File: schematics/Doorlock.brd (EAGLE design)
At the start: 79.7 x 80 mm, 33 parts, among them IC1 AT90S2313P, IC2 MAX232, K1 FRS1B, K2 FRS1B

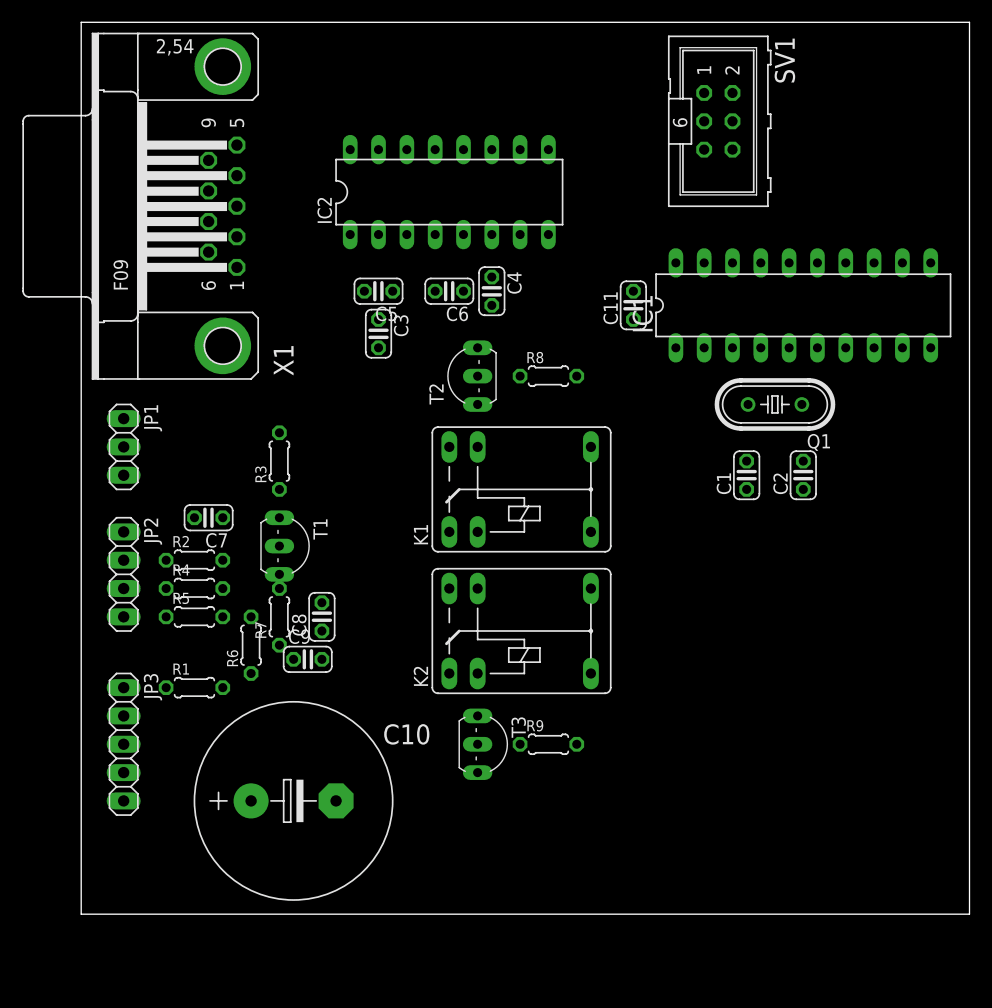
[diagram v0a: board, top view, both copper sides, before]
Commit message: First steps towards Raspberry Pi doorlock hat
Signed-off-by: Ralf Ramsauer <ralf@binary-kitchen.de>
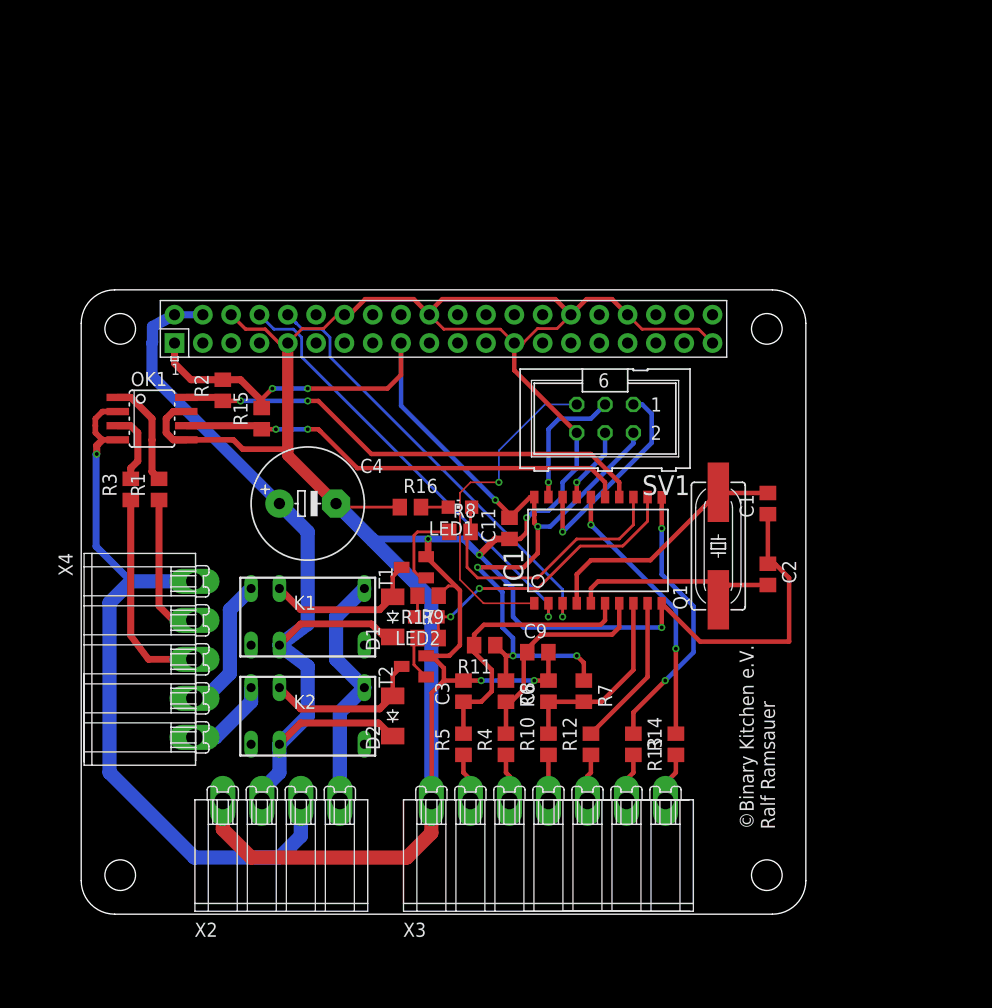
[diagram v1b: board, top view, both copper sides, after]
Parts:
- removed C10: (no value), rcl:E7,5-18
- removed C5, C6: 1u, rcl:C025-024X044
- removed C7: 100n, rcl:C025-024X044
- removed IC2: MAX232, maxim:DIL16
- removed JP1: (no value), pinhead:1X03
- removed JP2: (no value), pinhead:1X04
- removed JP3: (no value), pinhead:1X05
- removed T3: (no value), transistor:TO92-CBE
- added D1, D2: CGRM4002-G, diode:SOD-123_MINI-SMA
- added LED1, LED2: (no value), led:CHIP-LED0805
- added OK1: ILD205, optocoupler:SOIC08
- added R10, R15: 1k, rcl:R0805
- added R11: 10k, rcl:R0805
- added R12, R13, R14, R16, R17: 100, rcl:R0805
- added X2: RIA182-04, con-ria182:RIA182-04
- added X3: RIA182-07, con-ria182:RIA182-07
- added X4: RIA182-05, con-ria182:RIA182-05
- C1, C11, C2, C8, C9: device rcl:C025-024X044 -> rcl:C0805
- C3: value 1u -> 100n; device rcl:C025-024X044 -> rcl:C0805
- C4: value 1u -> RAD FC 1.200/16; device rcl:C025-024X044 -> rcl:E5-10,5
- IC1: value AT90S2313P -> AT90S2313S; device atmel:DIL20 -> atmel:SO20L
- K1, K2: value FRS1B -> G5V1; device relay:FRS1B -> relay:G5V1
- Q1: device crystal:HC49/S -> crystal:HC49UP
- R1, R4, R5, R6, R7, R8, R9: device rcl:0204/5 -> rcl:R0805
- R2, R3: value 10k -> 1k; device rcl:0204/5 -> rcl:R0805
- T1, T2: device transistor:TO92-CBE -> transistor:SOT23-BEC
- X1: value (none) -> RASPI_BOARD_B+#_H; device con-subd:F09HP -> raspberrypi_bastelstube_v13:RASPI_BOARD_B+HAT
- moved X1 64.8 mm to (0.00, 0.00), turned to 0 degrees
- moved C3 33.0 mm to (34.3, 20.0), turned to 90 degrees
- moved R4 31.2 mm to (38.1, 15.2), turned to 90 degrees
- moved IC1 28.8 mm to (45.7, 33.0)
- moved SV1 28.5 mm to (47.0, 44.5), turned to 180 degrees
- moved R7 28.1 mm to (45.1, 20.0), turned to 270 degrees
- moved R5 26.7 mm to (34.3, 15.2), turned to 90 degrees
- moved T2 26.7 mm to (29.8, 22.2)
- moved C4 25.2 mm to (20.3, 36.8), turned to 0 degrees
- moved R6 23.2 mm to (38.1, 20.0), turned to 270 degrees
- moved C11 22.9 mm to (38.4, 34.6)
- moved C8 21.4 mm to (41.9, 20.0)
- moved C9 20.6 mm to (41.0, 23.5)
- moved K1 19.1 mm to (20.3, 26.7)
- moved R1 18.1 mm to (6.99, 38.1), turned to 90 degrees
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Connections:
- removed net 12VAC: JP3.3
- removed net BUTTON_LOCK: C9.1, IC1.6, R5.2, R6.2
- removed net BUTTON_UNLOCK: C8.1, IC1.7, R4.2, R7.2
- removed net N$15: C6.1, IC2.5
- removed net N$18: C5.2, IC2.1
- removed net N$19: JP3.1, R1.1
- removed net N$23: K2.S
- removed net STATUS: IC1.14, R1.2
- new net +5V: C4.+, D1.C, D2.C, K1.2, K2.2, X1.2, X1.4, X2.2
- new net BUTTON_GREEN: C8.1, IC1.8, R10.2, R7.2
- new net BUTTON_RED: C3.1, IC1.6, R11.2, R5.2
- new net BUTTON_YELLOW: C9.1, IC1.7, R4.2, R6.2
- new net GND2: OK1.2, OK1.4, X2.3, X4.1
- new net LED_GREEN: IC1.16, R14.2
- new net LED_RED: IC1.9, R12.2
- new net LED_YELLOW: IC1.11, R13.1
- new net RXD: IC1.2, X1.8
- new net TUERSTATUS: IC1.14, OK1.8, R2.1
- new net TXD: IC1.3, X1.10
- net +12V: now also K1.6, K2.6, X2.4; no longer JP3.2
- net BOLZEN: now also IC1.13, LED1.A; no longer IC1.12
- net BOLZEN_OUT: now also K1.10, X4.4; no longer JP2.3, K1.S
- net EMERGENCY_UNLOCK: now also IC1.15, OK1.6, R15.1; no longer IC1.8, R3.1, T1.C
- net GND: now also C3.2, C4.-, OK1.5, OK1.7, R16.1, R17.1, X1.14, X1.20, X1.25, X1.30, X1.34, X1.39, X1.6, X1.9, X2.1, X3.1; no longer C10.-, C4.2, C7.1, IC2.15, JP1.1, JP2.1, JP3.5, T3.E, X1.5
- net N$10: now also R1.1, X4.2; no longer JP2.2, R2.1
- net N$11: now also R13.2, X3.6; no longer C3.1, IC2.2
- net N$12: now also R14.1, X3.7; no longer C4.1, IC2.6
- net N$13: now also R3.1, X4.3; no longer IC1.2, IC2.11
- net N$14: now also OK1.1, R1.2; no longer IC1.3, IC2.12
- net N$16: now also LED1.C, R16.2; no longer C6.2, IC2.4
- net N$17: now also LED2.C, R17.2; no longer C5.1, IC2.3
- net N$20: now also X3.3; no longer JP1.2
- net N$21: now also X3.2; no longer JP1.3
- net N$24: now also D2.A, K2.9, T2.C; no longer K2.2, T3.C
- net N$25: now also D1.A, K1.9, T1.C; no longer K1.1, T2.C
- net N$27: now also T1.B; no longer T2.B
- net N$28: now also T2.B; no longer T3.B
- net N$4: now also OK1.3, R3.2; no longer C7.2, R2.2, T1.B
- net N$8: now also R10.1, X3.4; no longer IC2.14, X1.2
- net N$9: now also R12.1, X3.5; no longer IC2.13, X1.3
- net SCHNAPPER: now also IC1.12, LED2.A; no longer IC1.13
- net SCHNAPPER_OUT: now also K2.10, X4.5; no longer JP2.4
- net VCC: now also R11.1, R15.2, R2.2, X1.1, X1.17; no longer C10.+, C3.2, IC2.16, JP3.4, K1.2, K2.1, R3.2
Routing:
- net GND: track 0.00 -> 285.9 mm, vias 0 -> 6
- net VCC: track 0.00 -> 96.1 mm, vias 0 -> 7
- net +5V: track 0.00 -> 80.2 mm
- net GND2: track 0.00 -> 68.0 mm, vias 0 -> 1
- net TUERSTATUS: track 0.00 -> 43.3 mm, vias 0 -> 2
- net EMERGENCY_UNLOCK: track 0.00 -> 41.0 mm, vias 0 -> 2
- net RXD: track 0.00 -> 40.1 mm, vias 0 -> 1
- net TXD: track 0.00 -> 39.6 mm, vias 0 -> 1
- net N$3: track 0.00 -> 30.8 mm, vias 0 -> 1
- net SCHNAPPER: track 0.00 -> 26.4 mm, vias 0 -> 2
- net BOLZEN: track 0.00 -> 25.3 mm
- net BUTTON_RED: track 0.00 -> 25.3 mm
- net LED_YELLOW: track 0.00 -> 24.6 mm, vias 0 -> 2
- net LED_GREEN: track 0.00 -> 24.4 mm, vias 0 -> 2
- net N$6: track 0.00 -> 22.9 mm
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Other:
- board size 79.7 x 80 mm -> 65 x 56 mm
- board text added: "©Binary Kitchen e.V. Ralf Ramsauer"

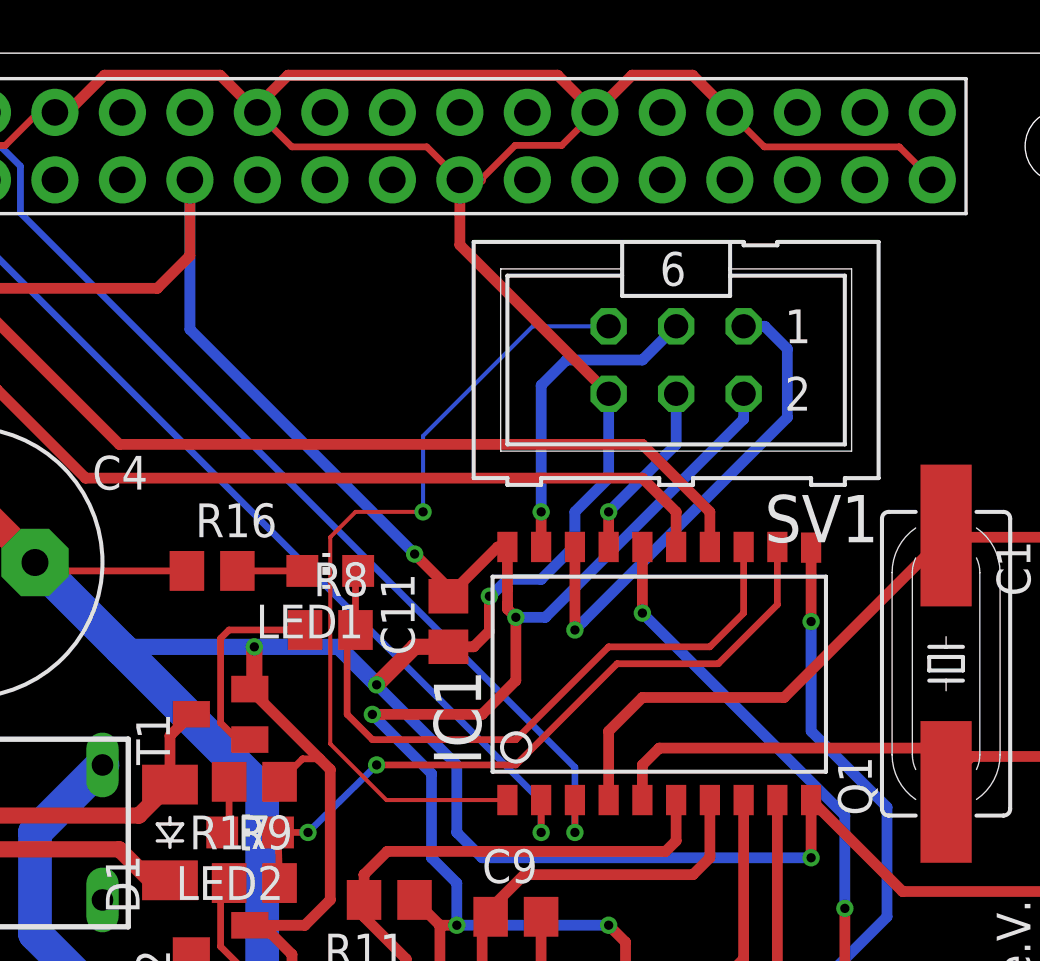
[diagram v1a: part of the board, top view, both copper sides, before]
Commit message: Remove ISP adapter
Let's flash the device with the Raspberry Pi :-)
... But add an Jumper for the reset line.

Signed-off-by: Ralf Ramsauer <ralf@binary-kitchen.de>
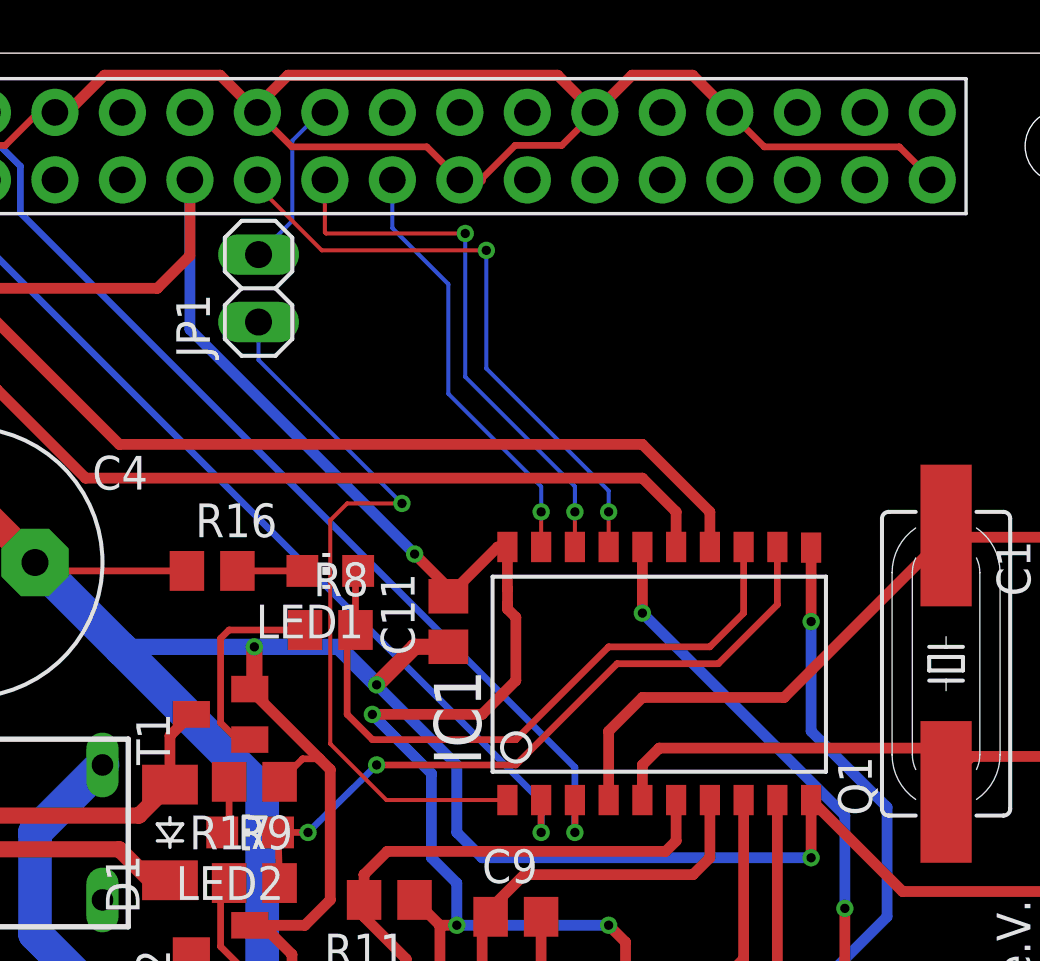
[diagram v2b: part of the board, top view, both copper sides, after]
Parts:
- removed SV1: (no value), con-harting-ml:ML6
- added JP1: (no value), pinhead:1X02
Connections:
- removed net N$2: IC1.19, SV1.3
- removed net N$3: IC1.1, SV1.5
- removed net N$5: IC1.17, SV1.4
- new net MISO: IC1.18, X1.21
- new net MOSI: IC1.17, X1.19
- new net RESET: JP1.2, X1.22
- new net SCK: IC1.19, X1.23
- net GND: no longer SV1.6
- net N$1: now also IC1.1, JP1.1; no longer IC1.18, SV1.1
- net VCC: no longer SV1.2
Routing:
- net N$3: track 30.8 -> 0.00 mm, vias 1 -> 0
- net GND: track 285.9 -> 262.2 mm, vias 6 -> 5
- net MOSI: track 0.00 -> 22.9 mm, vias 0 -> 2
- net MISO: track 0.00 -> 20.8 mm, vias 0 -> 2
- net SCK: track 0.00 -> 16.1 mm, vias 0 -> 1
- net VCC: track 96.1 -> 83.5 mm, vias 7 -> 6
- net N$2: track 12.1 -> 0.00 mm, vias 1 -> 0
- net N$1: track 19.0 -> 28.0 mm
- net N$5: track 6.82 -> 0.00 mm, vias 1 -> 0
- net RESET: track 0.00 -> 6.48 mm

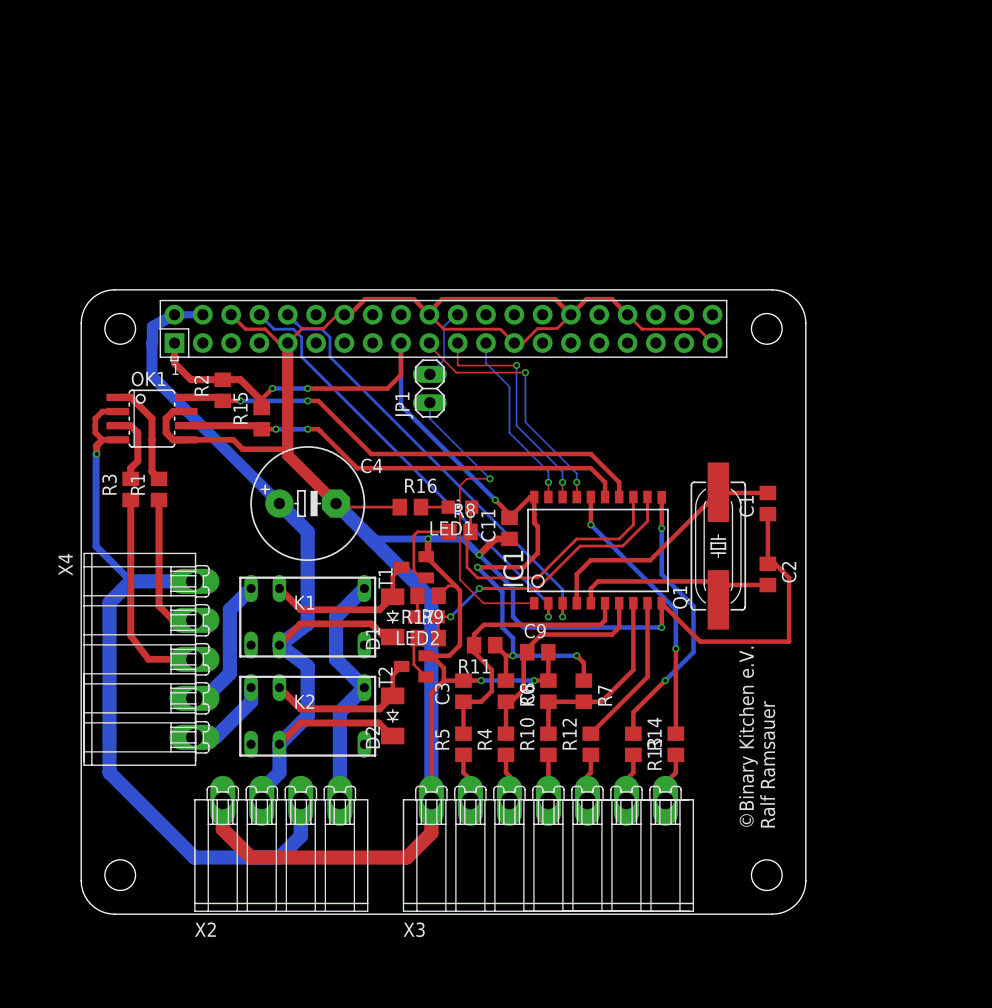
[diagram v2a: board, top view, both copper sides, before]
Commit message: schematics: improve schematics
  - Use RJ45 instead for buttons/LEDs
  - Use SMD capacitor

Signed-off-by: Ralf Ramsauer <ralf@binary-kitchen.de>
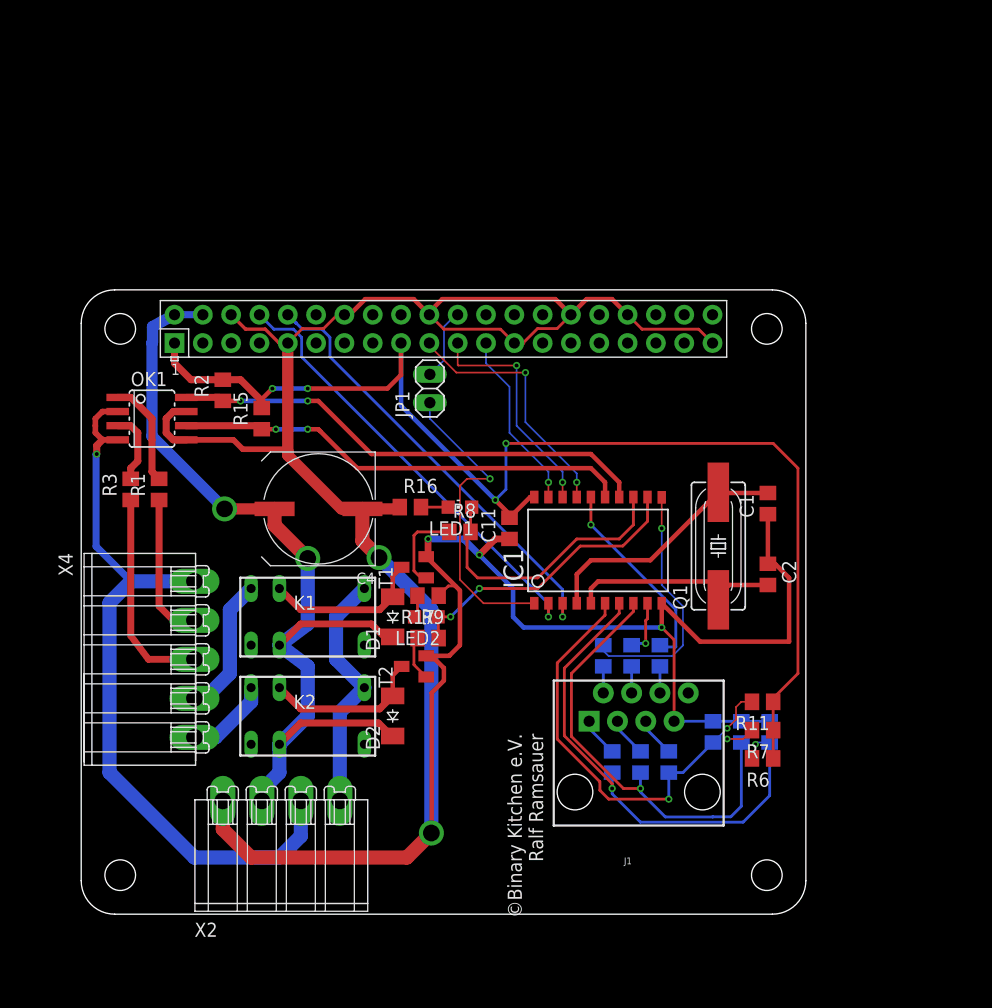
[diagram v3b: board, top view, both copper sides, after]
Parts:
- removed X3: RIA182-07, con-ria182:RIA182-07
- added J1: RJ45, SparkFun-Connectors:RJ45-8
- C4: value RAD FC 1.200/16 -> VF1000/10K-G; device rcl:E5-10,5 -> rcl:UD-10X10_NICHICON
- moved R11 25.4 mm to (61.1, 19.1)
- moved R6 23.8 mm to (61.1, 14.0), turned to 180 degrees
- moved C3 22.7 mm to (56.7, 16.4), flipped to the bottom
- moved C9 22.0 mm to (61.8, 16.4), flipped to the bottom, turned to 90 degrees
- moved R5 18.5 mm to (52.7, 13.7), flipped to the bottom, turned to 270 degrees
- moved C8 17.7 mm to (59.2, 16.4), flipped to the bottom
- moved R7 16.4 mm to (61.1, 16.5), turned to 180 degrees
- moved R4 9.66 mm to (47.6, 13.7), flipped to the bottom, turned to 270 degrees
- moved R12 8.74 mm to (49.4, 23.2), flipped to the bottom
- moved R10 8.41 mm to (50.2, 13.7), flipped to the bottom, turned to 270 degrees
- moved R13 8.38 mm to (46.8, 23.2), flipped to the bottom
- moved R14 8.07 mm to (51.9, 23.2), flipped to the bottom
- moved C4 1.06 mm to (21.3, 36.4), turned to 180 degrees
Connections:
- removed net N$12: R14.1, X3.7
- new net N$2: J1.6, R14.1
- net GND: now also J1.7; no longer X3.1
- net N$11: now also J1.2; no longer X3.6
- net N$20: now also J1.1; no longer X3.3
- net N$21: now also J1.5; no longer X3.2
- net N$8: now also J1.3; no longer X3.4
- net N$9: now also J1.4; no longer X3.5
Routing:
- net VCC: track 83.5 -> 110.3 mm, vias 6 -> 4
- net BUTTON_GREEN: track 17.6 -> 44.2 mm, vias 0 -> 2
- net BUTTON_YELLOW: track 19.9 -> 46.0 mm, vias 0 -> 2
- net BUTTON_RED: track 25.3 -> 39.8 mm, vias 0 -> 2
- net LED_RED: track 13.8 -> 5.00 mm, vias 0 -> 1
- net LED_GREEN: track 24.4 -> 18.1 mm, vias 2 -> 1
- net N$12: track 4.52 -> 0.00 mm
- net +5V: track 80.2 -> 82.9 mm, vias 0 -> 2
- net N$2: track 0.00 -> 2.38 mm
- net LED_YELLOW: track 24.6 -> 22.3 mm, vias 2 -> 1
- net GND: track 262.2 -> 264.3 mm
- net N$11: track 4.39 -> 2.38 mm
- net N$9: track 4.26 -> 2.38 mm
- net N$21: track 4.39 -> 3.56 mm
- net N$20: track 4.26 -> 3.56 mm
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
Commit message: schematics: Update Resistor values
Signed-off-by: Ralf Ramsauer <ralf@binary-kitchen.de>
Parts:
- R12, R13: value 100 -> 220
- R14: value 100 -> 0
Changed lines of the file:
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@@
 <element name="R10" library="rcl" package="R0805" value="1k" x="50.165" y="13.6525" rot="MR270"/>
 <element name="R11" library="rcl" package="R0805" value="10k" x="61.11875" y="19.05" rot="R180"/>
-<element name="R12" library="rcl" package="R0805" value="100" x="49.37125" y="23.1775" rot="MR90"/>
-<element name="R13" library="rcl" package="R0805" value="100" x="46.83125" y="23.1775" rot="MR270"/>
-<element name="R14" library="rcl" package="R0805" value="100" x="51.91125" y="23.1775" rot="MR90"/>
+<element name="R12" library="rcl" package="R0805" value="220" x="49.37125" y="23.1775" rot="MR90"/>
+<element name="R13" library="rcl" package="R0805" value="220" x="46.83125" y="23.1775" rot="MR270"/>
+<element name="R14" library="rcl" package="R0805" value="0" x="51.91125" y="23.1775" rot="MR90"/>
 <element name="R15" library="rcl" package="R0805" value="1k" x="16.1925" y="44.45" rot="R90"/>
 <element name="R2" library="rcl" package="R0805" value="1k" x="12.7" y="46.99" rot="R90"/>
